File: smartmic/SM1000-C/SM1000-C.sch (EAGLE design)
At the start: 199 parts, among them CN1 HDR100-3, CN10 ST-3509, CN11 HDR100-3, CN12 HRS-A3C-16DA, CN2 MOLEX-MINI-B-SMT, CN3 RASM722PX, CN4 RJ-45, CN5 ST-3509, CN6 ST-3509, CN7 ST-3509, CN8 ST-3509, CN9 ST-3509, J1 JMP-2PIN, J3 JMP-2PIN, J4 JMP-2PIN, P1 TPAD50, P10 TPAD50, P11 TPAD50, P12 TPAD50, P13 TPAD50, P14 TPAD50, P15 TPAD50, P16 TPAD50, P17 TPAD50, P18 TPAD50, P19 TPAD50, P2 TPAD50, P20 TPAD50, P3 TPAD50, P4 TPAD50, P5 TPAD50, P6 TPAD50, P7 TPAD50, P8 TPAD50, P9 TPAD50, SW1 SW-BOURNS-7914S, SW2 SW-BOURNS-7914S, SW3 DPDT, SW4 SW-BOURNS-7914S, SW5 SW-BOURNS-7914J, T1 SM-LP-5001, T2 SM-LP-5001, U1 STM32F405, U2 LD3985M33R, U3 STMPS2141, U4 EMIF02-USB03F2, U5 TPS54329E, U6 LMV341, U7 LMV341, U8 LM386M-1, U9 LMV341

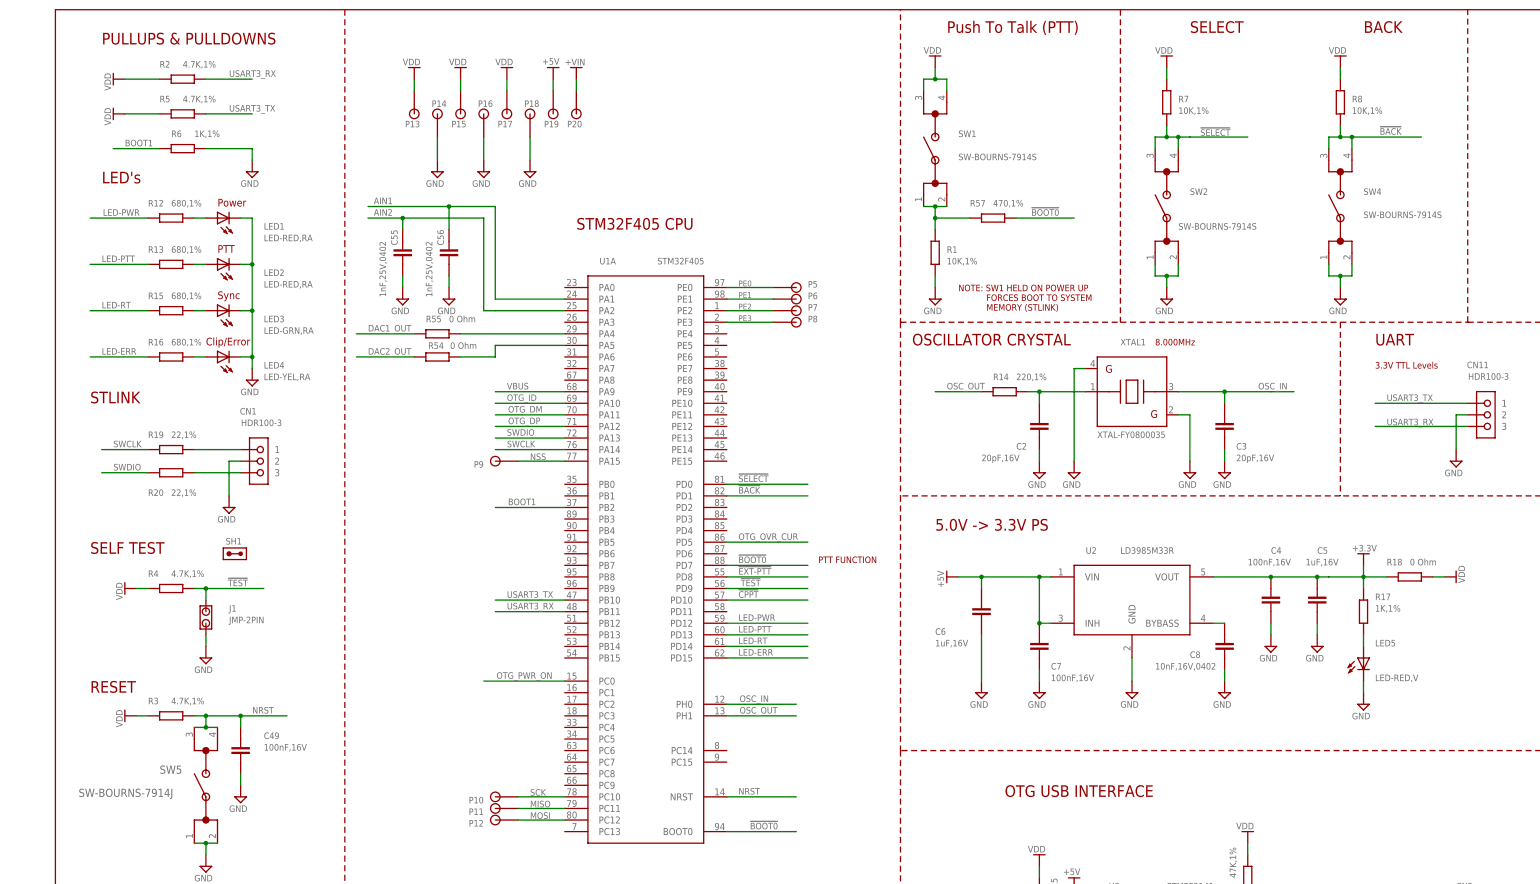
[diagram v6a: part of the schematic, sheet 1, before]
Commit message: Update schematic & BOM to reflect latest part changes - rgb
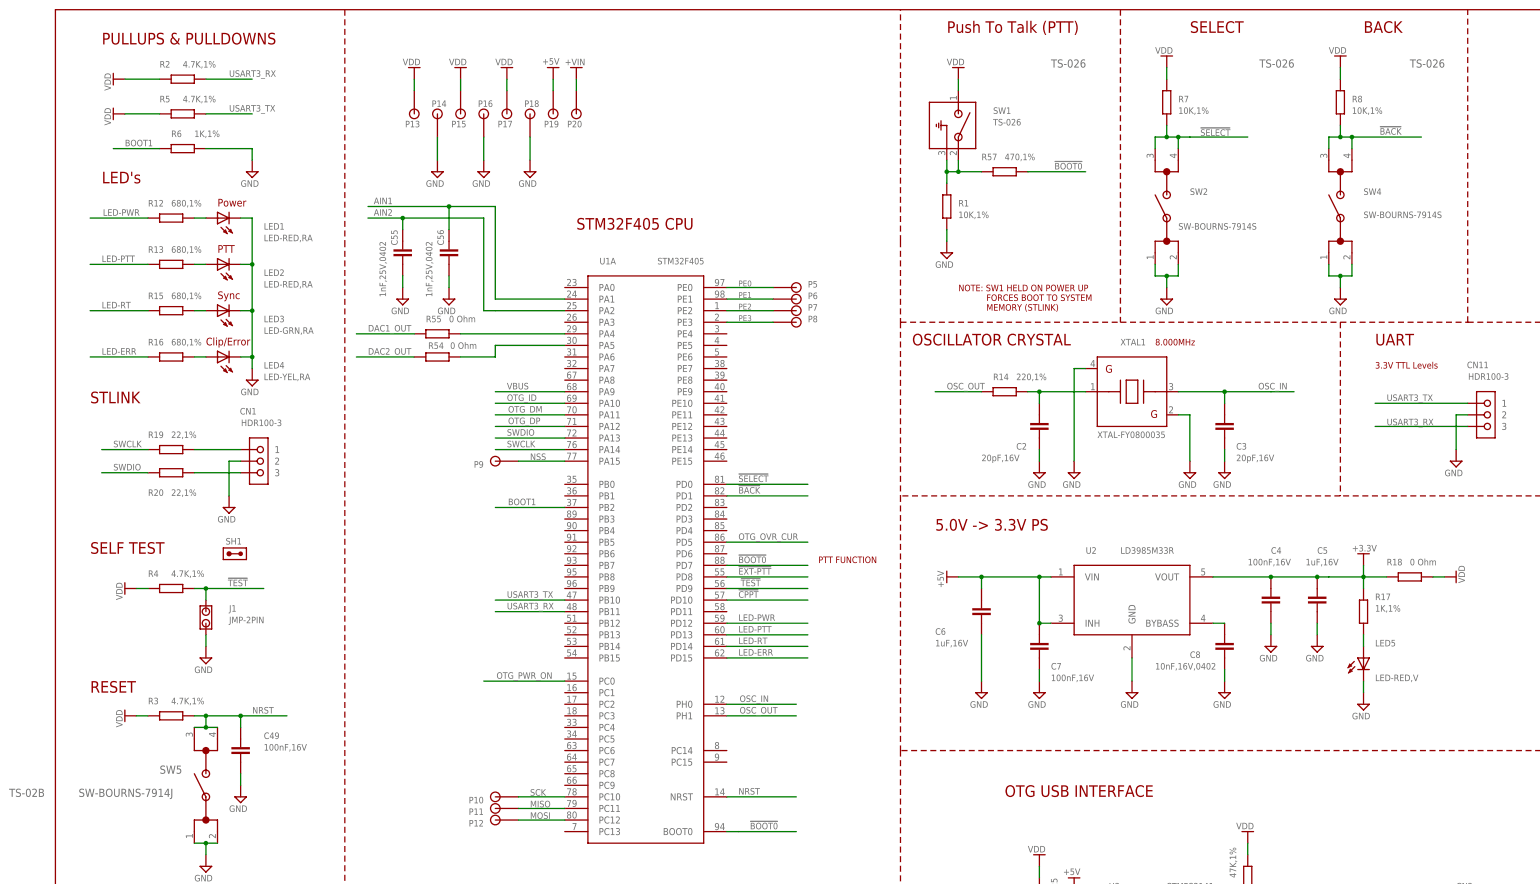
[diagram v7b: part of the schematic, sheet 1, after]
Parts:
- SW1: value SW-BOURNS-7914S -> TS-026; device SM1000-2L-70x90:SW-BOURNS-7914S -> _RoweTel:TS-026
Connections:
- net GND: now also CN10.A
- net N$14: now also SW1.2, SW1.3; no longer SW1.P$1, SW1.P$2
- net N$75: now also CN8.B
- net VDD: now also SW1.1; no longer SW1.P$3, SW1.P$4
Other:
- note added: "TS-026"
- note added: "TS-02B"
- note removed: "Release for Production"
- moved on the sheet: R1, R57, SW1
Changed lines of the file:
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@@
 <part name="V115" library="A-SUPPLY2" deviceset="VDD" device=""/>
 <part name="CN1" library="_Coherix" deviceset="HDR100-3" device=""/>
-<part name="SW1" library="SM1000-2L-70x90" deviceset="SW-BOURNS-7914S" device=""/>
 <part name="R1" library="AA-ipc-7351-resistor" deviceset="RESISTOR_" device="0603" value="10K,1%"/>
 <part name="V18" library="A-SUPPLY2" deviceset="GND" device=""/>
@@
 <part name="CN10" library="_RoweTel" deviceset="ST-3509" device=""/>
 <part name="CN12" library="_RoweTel" deviceset="HRS-A3C-16DA" device=""/>
+<part name="SW1" library="_RoweTel" deviceset="TS-026" device=""/>
 </parts>
 <sheets>
@@
 <wire x1="420.37" y1="263.906" x2="420.37" y2="218.44" width="0.1524" layer="94"/>
 <wire x1="425.45" y1="263.906" x2="425.45" y2="218.186" width="0.1524" layer="94"/>
+<text x="-10.16" y="106.68" size="1.778" layer="95" ratio="10">TS-02B</text>
+<text x="218.44" y="266.7" size="1.778" layer="95" ratio="10">TS-026</text>
+<text x="264.16" y="266.7" size="1.778" layer="95" ratio="10">TS-026</text>
+<text x="297.18" y="266.7" size="1.778" layer="95" ratio="10">TS-026</text>
 </plain>
 <instances>
@@
 <attribute name="VALUE" x="40.7239" y="189.463" size="1.4224" layer="96" ratio="9" rot="MR180"/>
 </instance>
-<instance part="SW1" gate="G$1" x="193.04" y="241.3" smashed="yes" rot="R90">
-<attribute name="NAME" x="198.12" y="251.46" size="1.4224" layer="95" ratio="10"/>
-<attribute name="VALUE" x="198.12" y="246.38" size="1.4224" layer="96" ratio="10"/>
-</instance>
-<instance part="R1" gate="G$1" x="193.04" y="226.06" smashed="yes" rot="R90">
-<attribute name="NAME" x="195.58" y="226.06" size="1.4224" layer="95" ratio="9"/>
-<attribute name="VALUE" x="195.58" y="223.52" size="1.4224" layer="96" ratio="9"/>
-</instance>
-<instance part="V18" gate="GND" x="193.04" y="215.9"/>
-<instance part="V19" gate="G$1" x="193.04" y="266.7" smashed="yes">
-<attribute name="VALUE" x="190.5" y="269.748" size="1.4224" layer="95" ratio="9"/>
+<instance part="R1" gate="G$1" x="195.58" y="236.22" smashed="yes" rot="R90">
+<attribute name="NAME" x="198.12" y="236.22" size="1.4224" layer="95" ratio="9"/>
+<attribute name="VALUE" x="198.12" y="233.68" size="1.4224" layer="96" ratio="9"/>
+</instance>
+<instance part="V18" gate="GND" x="195.58" y="226.06"/>
+<instance part="V19" gate="G$1" x="198.12" y="264.16" smashed="yes">
+<attribute name="VALUE" x="195.58" y="267.208" size="1.4224" layer="95" ratio="9"/>
 </instance>
 <instance part="V12" gate="G$1" x="15.24" y="264.16" rot="R90"/>
@@
 <instance part="V125" gate="GND" x="76.2" y="215.9"/>
 <instance part="V126" gate="GND" x="86.36" y="215.9"/>
-<instance part="R57" gate="G$1" x="205.74" y="233.68" smashed="yes" rot="R180">
-<attribute name="NAME" x="200.66" y="236.22" size="1.4224" layer="95" ratio="9"/>
-<attribute name="VALUE" x="205.74" y="236.22" size="1.4224" layer="96" ratio="9"/>
+<instance part="R57" gate="G$1" x="208.28" y="243.84" smashed="yes" rot="R180">
+<attribute name="NAME" x="203.2" y="246.38" size="1.4224" layer="95" ratio="9"/>
+<attribute name="VALUE" x="208.28" y="246.38" size="1.4224" layer="96" ratio="9"/>
 </instance>
 <instance part="R18" gate="G$1" x="297.18" y="154.94" smashed="yes">
@@
 </instance>
 <instance part="SPKR1" gate="G$1" x="360.68" y="48.26"/>
+<instance part="SW1" gate="G$1" x="193.04" y="254" smashed="yes" rot="R270">
+<attribute name="NAME" x="205.74" y="256.54" size="1.4224" layer="95" ratio="10"/>
+<attribute name="VALUE" x="205.74" y="254" size="1.4224" layer="95" ratio="10"/>
+</instance>
 </instances>
 <busses>
@@
 </segment>
 <segment>
-<pinref part="SW1" gate="G$1" pin="P$3"/>
-<wire x1="190.5" y1="261.62" x2="190.5" y2="264.16" width="0.1524" layer="91"/>
-<wire x1="190.5" y1="264.16" x2="193.04" y2="264.16" width="0.1524" layer="91"/>
-<pinref part="SW1" gate="G$1" pin="P$4"/>
-<wire x1="193.04" y1="264.16" x2="195.58" y2="264.16" width="0.1524" layer="91"/>
-<wire x1="195.58" y1="264.16" x2="195.58" y2="261.62" width="0.1524" layer="91"/>
-<wire x1="193.04" y1="264.16" x2="193.04" y2="266.7" width="0.1524" layer="91"/>
-<pinref part="V19" gate="G$1" pin="VDD"/>
-<junction x="193.04" y="264.16"/>
-</segment>
-<segment>
 <pinref part="R2" gate="G$1" pin="1"/>
 <wire x1="22.86" y1="264.16" x2="15.24" y2="264.16" width="0.1524" layer="91"/>
@@
 <wire x1="281.94" y1="264.16" x2="281.94" y2="266.7" width="0.1524" layer="91"/>
 </segment>
+<segment>
+<wire x1="198.12" y1="264.16" x2="198.12" y2="261.62" width="0.1524" layer="91"/>
+<pinref part="V19" gate="G$1" pin="VDD"/>
+<pinref part="SW1" gate="G$1" pin="1"/>
+</segment>
 </net>
 <net name="BOOT1" class="0">
@@
 <segment>
 <pinref part="R1" gate="G$1" pin="1"/>
-<wire x1="193.04" y1="220.98" x2="193.04" y2="218.44" width="0.1524" layer="91"/>
+<wire x1="195.58" y1="231.14" x2="195.58" y2="228.6" width="0.1524" layer="91"/>
 <pinref part="V18" gate="GND" pin="GND"/>
 </segment>
@@
 <segment>
 <pinref part="R57" gate="G$1" pin="1"/>
-<wire x1="210.82" y1="233.68" x2="223.52" y2="233.68" width="0.1524" layer="91"/>
-<label x="214.122" y="234.188" size="1.4224" layer="95" ratio="10"/>
+<wire x1="213.36" y1="243.84" x2="226.06" y2="243.84" width="0.1524" layer="91"/>
+<label x="219.202" y="244.348" size="1.4224" layer="95" ratio="10"/>
 </segment>
 <segment>
@@
 <segment>
 <pinref part="R57" gate="G$1" pin="2"/>
-<wire x1="200.66" y1="233.68" x2="193.04" y2="233.68" width="0.1524" layer="91"/>
-<wire x1="193.04" y1="233.68" x2="193.04" y2="236.22" width="0.1524" layer="91"/>
+<wire x1="203.2" y1="243.84" x2="198.12" y2="243.84" width="0.1524" layer="91"/>
 <pinref part="R1" gate="G$1" pin="2"/>
-<wire x1="193.04" y1="233.68" x2="193.04" y2="231.14" width="0.1524" layer="91"/>
-<pinref part="SW1" gate="G$1" pin="P$1"/>
-<pinref part="SW1" gate="G$1" pin="P$2"/>
-<wire x1="190.5" y1="236.22" x2="193.04" y2="236.22" width="0.1524" layer="91"/>
-<junction x="193.04" y="236.22"/>
-<wire x1="193.04" y1="236.22" x2="195.58" y2="236.22" width="0.1524" layer="91"/>
-<junction x="193.04" y="233.68"/>
+<wire x1="198.12" y1="243.84" x2="195.58" y2="243.84" width="0.1524" layer="91"/>
+<wire x1="195.58" y1="243.84" x2="195.58" y2="241.3" width="0.1524" layer="91"/>
+<pinref part="SW1" gate="G$1" pin="3"/>
+<wire x1="195.58" y1="246.38" x2="195.58" y2="243.84" width="0.1524" layer="91"/>
+<pinref part="SW1" gate="G$1" pin="2"/>
+<wire x1="198.12" y1="246.38" x2="198.12" y2="243.84" width="0.1524" layer="91"/>
+<junction x="195.58" y="243.84"/>
+<junction x="198.12" y="243.84"/>
 </segment>
 </net>
@@
 <wire x1="353.06" y1="200.66" x2="353.06" y2="264.16" width="0.1524" layer="94" style="longdash"/>
 <wire x1="337.82" y1="200.66" x2="429.26" y2="200.66" width="0.1524" layer="95" style="longdash"/>
-<text x="355.6" y="264.16" size="1.4224" layer="94" ratio="10">10/13/14</text>
-<text x="368.3" y="264.16" size="1.4224" layer="94" ratio="10">Release for Production</text>
 <text x="419.1" y="264.16" size="1.4224" layer="94" ratio="10">C</text>
 <text x="424.18" y="264.16" size="1.4224" layer="94" ratio="10">RGB</text>
@@
 </segment>
 <segment>
-<wire x1="312.42" y1="220.98" x2="314.96" y2="220.98" width="0.1524" layer="91"/>
-<wire x1="314.96" y1="220.98" x2="314.96" y2="218.44" width="0.1524" layer="91"/>
-<pinref part="V109" gate="GND" pin="GND"/>
-</segment>
-<segment>
 <pinref part="C51" gate="G$1" pin="2"/>
 <wire x1="320.04" y1="223.52" x2="320.04" y2="218.44" width="0.1524" layer="91"/>
@@
 <wire x1="233.68" y1="10.16" x2="233.68" y2="12.7" width="0.1524" layer="91"/>
 </segment>
+<segment>
+<pinref part="CN10" gate="G$1" pin="A"/>
+<pinref part="V109" gate="GND" pin="GND"/>
+<wire x1="312.42" y1="220.98" x2="314.96" y2="220.98" width="0.1524" layer="91"/>
+<wire x1="314.96" y1="220.98" x2="314.96" y2="218.44" width="0.1524" layer="91"/>
+</segment>
 </net>
 <net name="N$38" class="0">
@@
 <wire x1="127" y1="55.88" x2="129.54" y2="55.88" width="0.1524" layer="91"/>
 <wire x1="129.54" y1="55.88" x2="132.08" y2="55.88" width="0.1524" layer="91"/>
-<wire x1="132.08" y1="43.18" x2="129.54" y2="43.18" width="0.1524" layer="91"/>
 <wire x1="129.54" y1="43.18" x2="129.54" y2="55.88" width="0.1524" layer="91"/>
 <junction x="129.54" y="55.88"/>
 <pinref part="CN8" gate="G$1" pin="C"/>
+<pinref part="CN8" gate="G$1" pin="B"/>
+<wire x1="132.08" y1="43.18" x2="129.54" y2="43.18" width="0.1524" layer="91"/>
 </segment>
 </net>

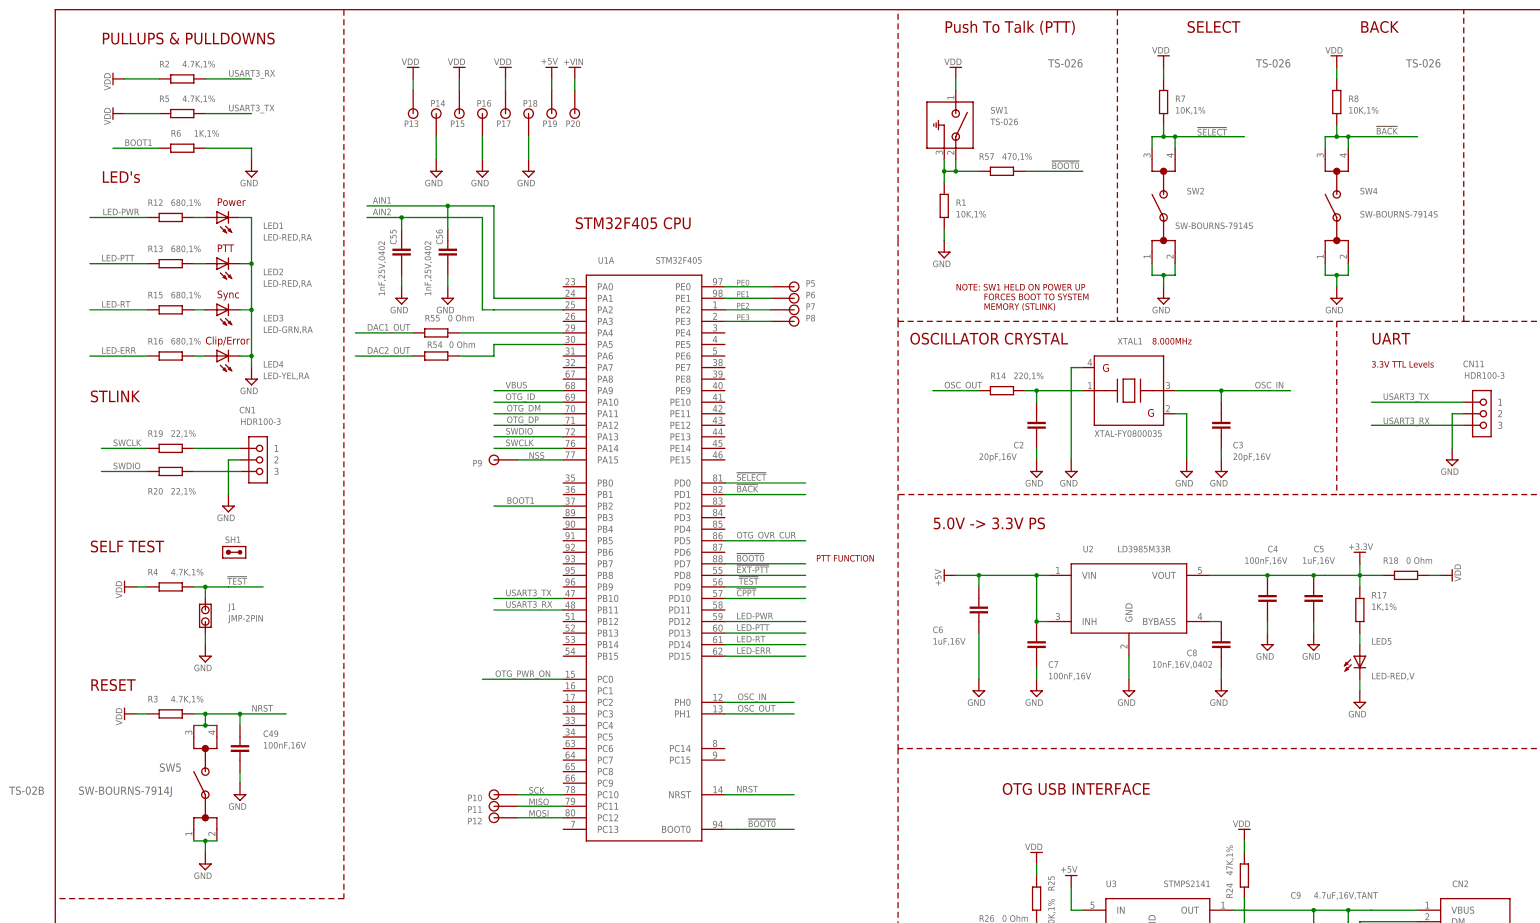
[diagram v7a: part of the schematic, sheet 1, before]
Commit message: Correct errors in last upload - RGB
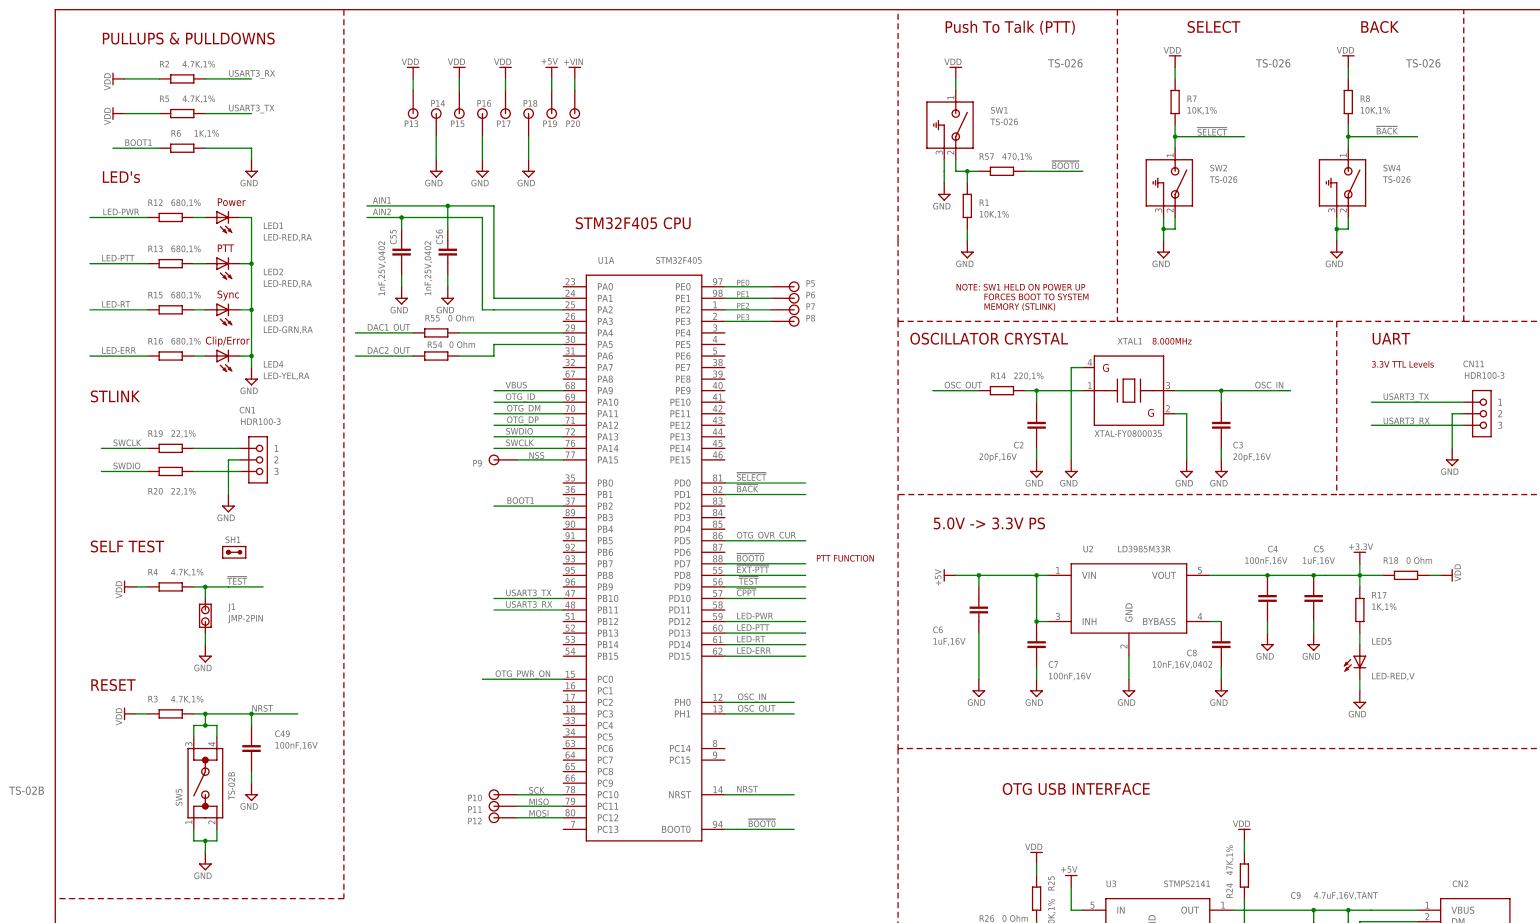
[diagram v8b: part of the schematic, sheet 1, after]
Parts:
- SW2, SW4: value SW-BOURNS-7914S -> TS-026; device SM1000-2L-70x90:SW-BOURNS-7914S -> _RoweTel:TS-026
- SW5: value SW-BOURNS-7914J -> TS-02B; device SM1000:SW-BOURNS-7914J -> _RoweTel:TS-02B
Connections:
- net !BACK!: now also SW4.1; no longer SW4.P$3, SW4.P$4
- net !SELECT!: now also SW2.1; no longer SW2.P$3, SW2.P$4
- net GND: now also SW1.3, SW2.2, SW2.3, SW4.2, SW4.3, SW5.1, SW5.2; no longer SW2.P$1, SW2.P$2, SW4.P$1, SW4.P$2, SW5.P$1, SW5.P$2
- net N$14: no longer SW1.3
- net NRST: now also SW5.3, SW5.4; no longer SW5.P$3, SW5.P$4
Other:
- moved on the sheet: C49, R1, R7, R8, SW2, SW4
